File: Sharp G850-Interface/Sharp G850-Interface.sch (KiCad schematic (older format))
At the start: 26 parts

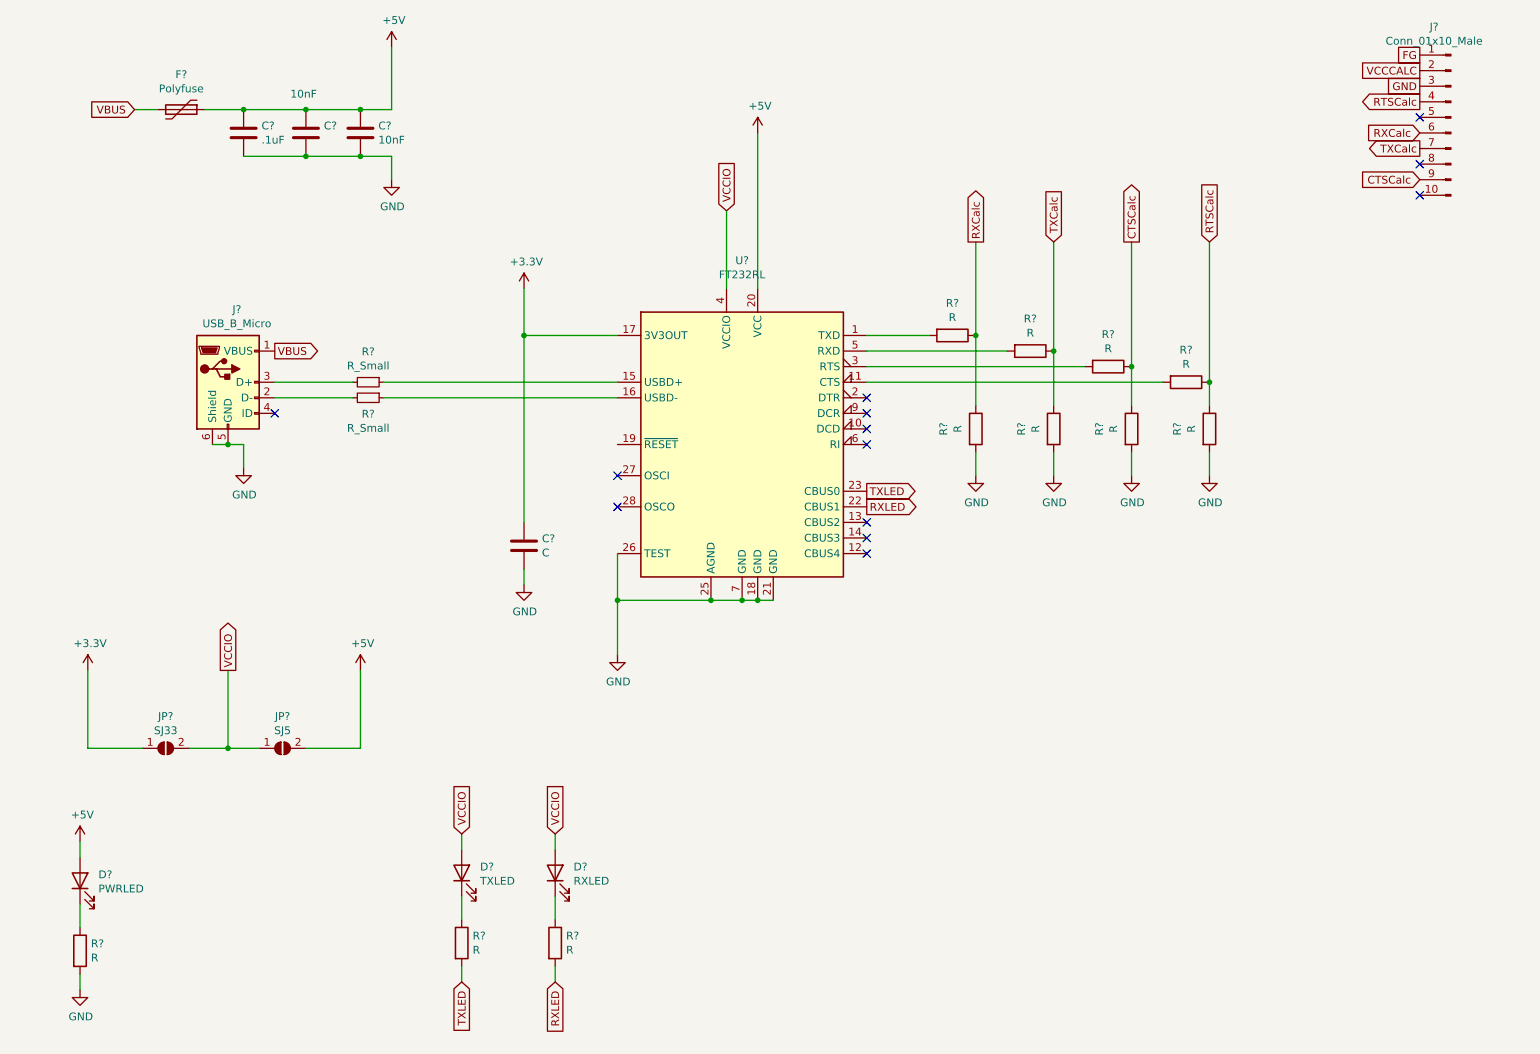
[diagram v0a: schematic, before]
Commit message: Finished G850 Schema
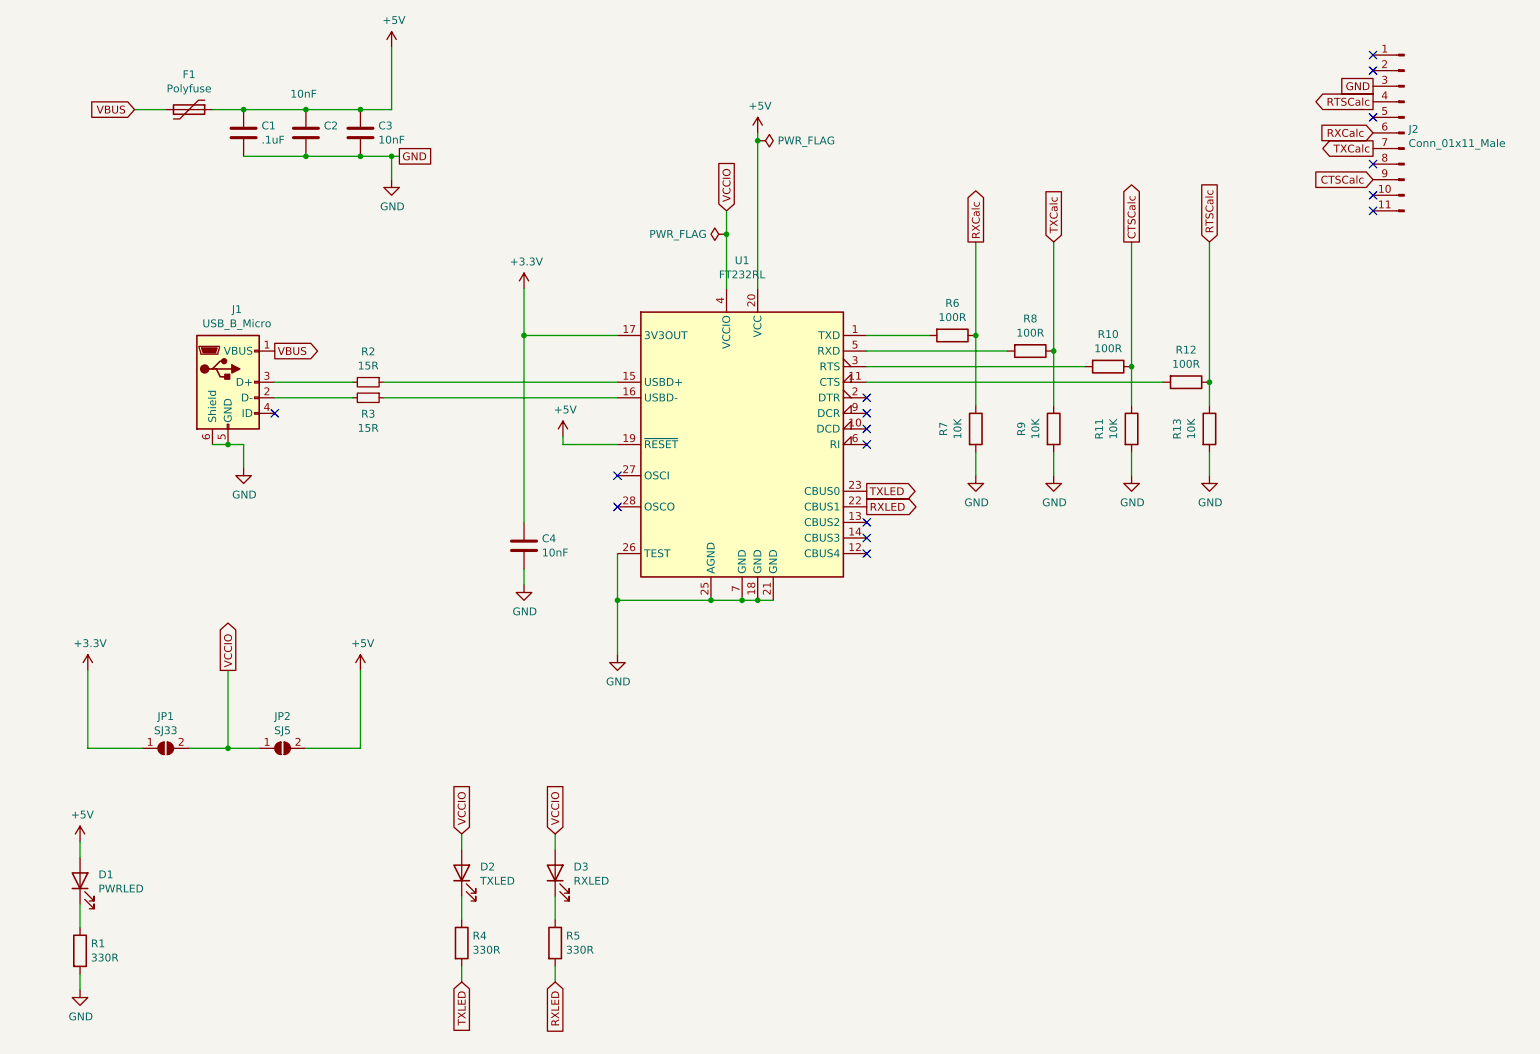
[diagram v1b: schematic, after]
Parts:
- removed J?: Conn_01x10_Male, symbol Connector:Conn_01x10_Male
- added J2: Conn_01x11_Male, symbol Connector:Conn_01x11_Male
- C4: renamed from C?; value C -> 10nF
- R1, R4, R5: renamed from R?; value R -> 330R
- R10, R12, R6, R8: renamed from R?; value R -> 100R
- R11, R13, R7, R9: renamed from R?; value R -> 10K
- R2, R3: renamed from R?; value R_Small -> 15R
- gave numbers to parts that had none: 11
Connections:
- net +5V: now also U1.19 (~RESET~)
- net CTSCalc: now also J2.9 (Pin_9)
- net GND: now also J2.3 (Pin_3)
- net RTSCalc: now also J2.4 (Pin_4)
- net RXCalc: now also J2.6 (Pin_6)
- net TXCalc: now also J2.7 (Pin_7)
- no-connect marks 13 -> 16
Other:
- moved on the sheet: F1

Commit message: Routage PCB Interface G850
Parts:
- added FB1: Ferrite_Bead_Small, Inductor_SMD:L_0805_2012Metric_Pad1.15x1.40mm_HandSolder, symbol Device:Ferrite_Bead_Small
- added J3: Conn_01x11_Male, Connector_PinHeader_2.54mm:PinHeader_1x11_P2.54mm_Vertical, symbol Connector:Conn_01x11_Male
- C1, C2, C3, C4: footprint (none) -> Capacitor_SMD:C_0805_2012Metric_Pad1.15x1.40mm_HandSolder
- D1, D2, D3: footprint (none) -> LED_SMD:LED_0805_2012Metric_Pad1.15x1.40mm_HandSolder
- F1: footprint (none) -> Resistor_SMD:R_1210_3225Metric_Pad1.42x2.65mm_HandSolder
- J1: footprint (none) -> Connector_USB:USB_Micro-B_Molex-105017-0001
- J2: footprint (none) -> Connector_PinHeader_2.54mm:PinHeader_1x11_P2.54mm_Horizontal
- JP1, JP2: footprint (none) -> Jumper:SolderJumper-2_P1.3mm_Open_RoundedPad1.0x1.5mm
- R1, R10, R11, R12, R13, R2, R3, R4, R5, R6, R7, R8, R9: footprint (none) -> Resistor_SMD:R_0805_2012Metric_Pad1.15x1.40mm_HandSolder
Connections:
- net +5V: now also FB1.1; no longer F1.1
- net CTSCalc: now also J3.9 (Pin_9)
- net GND: now also J3.3 (Pin_3)
- net RTSCalc: now also J3.4 (Pin_4)
- net RXCalc: now also J3.6 (Pin_6)
- net TXCalc: now also J3.7 (Pin_7)
- net USBD+: now reaches R2.1, U1.15 (USBD+)
- net USBD-: now reaches R3.1, U1.16 (USBD-)
- net D-: now reaches J1.2 (D-), R3.2
- net D+: now reaches J1.3 (D+), R2.2
- new net: F1.1, FB1.2
- no-connect marks 16 -> 22
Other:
- moved on the sheet: F1
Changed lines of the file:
@@
 F 0 "J1" H 2757 3567 50  0000 C CNN
 F 1 "USB_B_Micro" H 2757 3476 50  0000 C CNN
-F 2 "" H 2850 3050 50  0001 C CNN
+F 2 "Connector_USB:USB_Micro-B_Molex-105017-0001" H 2850 3050 50  0001 C CNN
 F 3 "~" H 2850 3050 50  0001 C CNN
 	1    2700 3100
@@
 L Device:Polyfuse F1
 U 1 1 5EB8FDB5
-P 2450 1350
-F 0 "F1" V 2225 1350 50  0000 C CNN
-F 1 "Polyfuse" V 2316 1350 50  0000 C CNN
-F 2 "" H 2500 1150 50  0001 L CNN
-F 3 "~" H 2450 1350 50  0001 C CNN
-	1    2450 1350
+P 2000 1350
+F 0 "F1" V 1775 1350 50  0000 C CNN
+F 1 "Polyfuse" V 1866 1350 50  0000 C CNN
+F 2 "Resistor_SMD:R_1210_3225Metric_Pad1.42x2.65mm_HandSolder" H 2050 1150 50  0001 L CNN
+F 3 "~" H 2000 1350 50  0001 C CNN
+	1    2000 1350
 	0    1    1    0
 $EndComp
@@
 F 0 "C1" H 2915 1546 50  0000 L CNN
 F 1 ".1uF" H 2915 1455 50  0000 L CNN
-F 2 "" H 2838 1350 50  0001 C CNN
+F 2 "Capacitor_SMD:C_0805_2012Metric_Pad1.15x1.40mm_HandSolder" H 2838 1350 50  0001 C CNN
 F 3 "~" H 2800 1500 50  0001 C CNN
 	1    2800 1500
@@
 F 0 "C2" H 3315 1546 50  0000 L CNN
 F 1 "10nF" H 3100 1750 50  0000 L CNN
-F 2 "" H 3238 1350 50  0001 C CNN
+F 2 "Capacitor_SMD:C_0805_2012Metric_Pad1.15x1.40mm_HandSolder" H 3238 1350 50  0001 C CNN
 F 3 "~" H 3200 1500 50  0001 C CNN
 	1    3200 1500
@@
 F 0 "C3" H 3665 1546 50  0000 L CNN
 F 1 "10nF" H 3665 1455 50  0000 L CNN
-F 2 "" H 3588 1350 50  0001 C CNN
+F 2 "Capacitor_SMD:C_0805_2012Metric_Pad1.15x1.40mm_HandSolder" H 3588 1350 50  0001 C CNN
 F 3 "~" H 3550 1500 50  0001 C CNN
 	1    3550 1500
@@
 Text GLabel 3000 2900 2    50   Output ~ 0
 VBUS
-Text GLabel 2100 1350 0    50   Input ~ 0
+Text GLabel 1650 1350 0    50   Input ~ 0
 VBUS
 Wire Wire Line
@@
 F 0 "JP2" H 3050 5655 50  0000 C CNN
 F 1 "SJ5" H 3050 5564 50  0000 C CNN
-F 2 "" H 3050 5450 50  0001 C CNN
+F 2 "Jumper:SolderJumper-2_P1.3mm_Open_RoundedPad1.0x1.5mm" H 3050 5450 50  0001 C CNN
 F 3 "~" H 3050 5450 50  0001 C CNN
 	1    3050 5450
@@
 F 0 "JP1" H 2300 5655 50  0000 C CNN
 F 1 "SJ33" H 2300 5564 50  0000 C CNN
-F 2 "" H 2300 5450 50  0001 C CNN
+F 2 "Jumper:SolderJumper-2_P1.3mm_Open_RoundedPad1.0x1.5mm" H 2300 5450 50  0001 C CNN
 F 3 "~" H 2300 5450 50  0001 C CNN
 	1    2300 5450
@@
 F 0 "R2" V 3404 3100 50  0000 C CNN
 F 1 "15R" V 3495 3100 50  0000 C CNN
-F 2 "" H 3600 3100 50  0001 C CNN
+F 2 "Resistor_SMD:R_0805_2012Metric_Pad1.15x1.40mm_HandSolder" H 3600 3100 50  0001 C CNN
 F 3 "~" H 3600 3100 50  0001 C CNN
 	1    3600 3100
@@
 F 0 "R3" V 3704 3200 50  0000 C CNN
 F 1 "15R" V 3795 3200 50  0000 C CNN
-F 2 "" H 3600 3200 50  0001 C CNN
+F 2 "Resistor_SMD:R_0805_2012Metric_Pad1.15x1.40mm_HandSolder" H 3600 3200 50  0001 C CNN
 F 3 "~" H 3600 3200 50  0001 C CNN
 	1    3600 3200
@@
 F 0 "D1" V 1789 6182 50  0000 R CNN
 F 1 "PWRLED" V 1698 6182 50  0000 R CNN
-F 2 "" H 1750 6300 50  0001 C CNN
+F 2 "LED_SMD:LED_0805_2012Metric_Pad1.15x1.40mm_HandSolder" H 1750 6300 50  0001 C CNN
 F 3 "~" H 1750 6300 50  0001 C CNN
 	1    1750 6300
@@
 F 0 "R1" H 1820 6796 50  0000 L CNN
 F 1 "330R" H 1820 6705 50  0000 L CNN
-F 2 "" V 1680 6750 50  0001 C CNN
+F 2 "Resistor_SMD:R_0805_2012Metric_Pad1.15x1.40mm_HandSolder" V 1680 6750 50  0001 C CNN
 F 3 "~" H 1750 6750 50  0001 C CNN
 	1    1750 6750
@@
 F 0 "D2" V 4239 6132 50  0000 R CNN
 F 1 "TXLED" V 4148 6132 50  0000 R CNN
-F 2 "" H 4200 6250 50  0001 C CNN
+F 2 "LED_SMD:LED_0805_2012Metric_Pad1.15x1.40mm_HandSolder" H 4200 6250 50  0001 C CNN
 F 3 "~" H 4200 6250 50  0001 C CNN
 	1    4200 6250
@@
 F 0 "R4" H 4270 6746 50  0000 L CNN
 F 1 "330R" H 4270 6655 50  0000 L CNN
-F 2 "" V 4130 6700 50  0001 C CNN
+F 2 "Resistor_SMD:R_0805_2012Metric_Pad1.15x1.40mm_HandSolder" V 4130 6700 50  0001 C CNN
 F 3 "~" H 4200 6700 50  0001 C CNN
 	1    4200 6700
@@
 F 0 "D3" V 4839 6132 50  0000 R CNN
 F 1 "RXLED" V 4748 6132 50  0000 R CNN
-F 2 "" H 4800 6250 50  0001 C CNN
+F 2 "LED_SMD:LED_0805_2012Metric_Pad1.15x1.40mm_HandSolder" H 4800 6250 50  0001 C CNN
 F 3 "~" H 4800 6250 50  0001 C CNN
 	1    4800 6250
@@
 F 0 "R5" H 4870 6746 50  0000 L CNN
 F 1 "330R" H 4870 6655 50  0000 L CNN
-F 2 "" V 4730 6700 50  0001 C CNN
+F 2 "Resistor_SMD:R_0805_2012Metric_Pad1.15x1.40mm_HandSolder" V 4730 6700 50  0001 C CNN
 F 3 "~" H 4800 6700 50  0001 C CNN
 	1    4800 6700
@@
 F 0 "R6" V 7143 2800 50  0000 C CNN
 F 1 "100R" V 7234 2800 50  0000 C CNN
-F 2 "" V 7280 2800 50  0001 C CNN
+F 2 "Resistor_SMD:R_0805_2012Metric_Pad1.15x1.40mm_HandSolder" V 7280 2800 50  0001 C CNN
 F 3 "~" H 7350 2800 50  0001 C CNN
 	1    7350 2800
@@
 F 0 "R8" V 7643 2900 50  0000 C CNN
 F 1 "100R" V 7734 2900 50  0000 C CNN
-F 2 "" V 7780 2900 50  0001 C CNN
+F 2 "Resistor_SMD:R_0805_2012Metric_Pad1.15x1.40mm_HandSolder" V 7780 2900 50  0001 C CNN
 F 3 "~" H 7850 2900 50  0001 C CNN
 	1    7850 2900
@@
 F 0 "R10" V 8143 3000 50  0000 C CNN
 F 1 "100R" V 8234 3000 50  0000 C CNN
-F 2 "" V 8280 3000 50  0001 C CNN
+F 2 "Resistor_SMD:R_0805_2012Metric_Pad1.15x1.40mm_HandSolder" V 8280 3000 50  0001 C CNN
 F 3 "~" H 8350 3000 50  0001 C CNN
 	1    8350 3000
@@
 F 0 "R12" V 8643 3100 50  0000 C CNN
 F 1 "100R" V 8734 3100 50  0000 C CNN
-F 2 "" V 8780 3100 50  0001 C CNN
+F 2 "Resistor_SMD:R_0805_2012Metric_Pad1.15x1.40mm_HandSolder" V 8780 3100 50  0001 C CNN
 F 3 "~" H 8850 3100 50  0001 C CNN
 	1    8850 3100
@@
 F 0 "R7" V 7293 3400 50  0000 C CNN
 F 1 "10K" V 7384 3400 50  0000 C CNN
-F 2 "" V 7430 3400 50  0001 C CNN
+F 2 "Resistor_SMD:R_0805_2012Metric_Pad1.15x1.40mm_HandSolder" V 7430 3400 50  0001 C CNN
 F 3 "~" H 7500 3400 50  0001 C CNN
 	1    7500 3400
@@
 F 0 "R9" V 7793 3400 50  0000 C CNN
 F 1 "10K" V 7884 3400 50  0000 C CNN
-F 2 "" V 7930 3400 50  0001 C CNN
+F 2 "Resistor_SMD:R_0805_2012Metric_Pad1.15x1.40mm_HandSolder" V 7930 3400 50  0001 C CNN
 F 3 "~" H 8000 3400 50  0001 C CNN
 	1    8000 3400
@@
 F 0 "R11" V 8293 3400 50  0000 C CNN
 F 1 "10K" V 8384 3400 50  0000 C CNN
-F 2 "" V 8430 3400 50  0001 C CNN
+F 2 "Resistor_SMD:R_0805_2012Metric_Pad1.15x1.40mm_HandSolder" V 8430 3400 50  0001 C CNN
 F 3 "~" H 8500 3400 50  0001 C CNN
 	1    8500 3400
@@
 F 0 "R13" V 8793 3400 50  0000 C CNN
 F 1 "10K" V 8884 3400 50  0000 C CNN
-F 2 "" V 8930 3400 50  0001 C CNN
+F 2 "Resistor_SMD:R_0805_2012Metric_Pad1.15x1.40mm_HandSolder" V 8930 3400 50  0001 C CNN
 F 3 "~" H 9000 3400 50  0001 C CNN
 	1    9000 3400
@@
 F 0 "C4" H 4715 4196 50  0000 L CNN
 F 1 "10nF" H 4715 4105 50  0000 L CNN
-F 2 "" H 4638 4000 50  0001 C CNN
+F 2 "Capacitor_SMD:C_0805_2012Metric_Pad1.15x1.40mm_HandSolder" H 4638 4000 50  0001 C CNN
 F 3 "~" H 4600 4150 50  0001 C CNN
 	1    4600 4150
@@
 F 0 "J2" H 10222 1524 50  0000 R CNN
 F 1 "Conn_01x11_Male" H 10222 1433 50  0000 R CNN
-F 2 "" H 10250 1500 50  0001 C CNN
+F 2 "Connector_PinHeader_2.54mm:PinHeader_1x11_P2.54mm_Horizontal" H 10250 1500 50  0001 C CNN
 F 3 "~" H 10250 1500 50  0001 C CNN
 	1    10250 1500
@@
 	2700 4950 2700 5450
 Wire Wire Line
-	2100 1350 2300 1350
-Wire Wire Line
-	2600 1350 2800 1350
-Connection ~ 2800 1350
+	1650 1350 1850 1350
 $Comp
 L power:PWR_FLAG #FLG0101
@@
 Wire Wire Line
 	5900 2150 5900 2000
+Text GLabel 10050 2450 0    50   UnSpc ~ 0
+GND
+Text GLabel 10050 2550 0    50   Output ~ 0
+RTSCalc
+Text GLabel 10050 2750 0    50   Input ~ 0
+RXCalc
+Text GLabel 10050 2850 0    50   Output ~ 0
+TXCalc
+Text GLabel 10050 3050 0    50   Input ~ 0
+CTSCalc
+NoConn ~ 10050 2650
+NoConn ~ 10050 2950
+NoConn ~ 10050 3150
+NoConn ~ 10050 2350
+NoConn ~ 10050 2250
+$Comp
+L Connector:Conn_01x11_Male J3
+U 1 1 5EC5BD70
+P 10250 2750
+F 0 "J3" H 10222 2774 50  0000 R CNN
+F 1 "Conn_01x11_Male" H 10222 2683 50  0000 R CNN
+F 2 "Connector_PinHeader_2.54mm:PinHeader_1x11_P2.54mm_Vertical" H 10250 2750 50  0001 C CNN
+F 3 "~" H 10250 2750 50  0001 C CNN
+	1    10250 2750
+	-1   0    0    -1
+$EndComp
+NoConn ~ 10050 3250
+$Comp
+L Device:Ferrite_Bead_Small FB1
+U 1 1 5EC5F7C4
+P 2550 1350
+F 0 "FB1" V 2313 1350 50  0000 C CNN
+F 1 "Ferrite_Bead_Small" V 2404 1350 50  0000 C CNN
+F 2 "Inductor_SMD:L_0805_2012Metric_Pad1.15x1.40mm_HandSolder" V 2480 1350 50  0001 C CNN
+F 3 "~" H 2550 1350 50  0001 C CNN
+	1    2550 1350
+	0    1    1    0
+$EndComp
+Wire Wire Line
+	2150 1350 2450 1350
+Wire Wire Line
+	2650 1350 2800 1350
+Connection ~ 2800 1350
+Text Label 3150 3100 0    50   ~ 0
+D+
+Text Label 3150 3200 0    50   ~ 0
+D-
+Text Label 4150 3100 0    50   ~ 0
+USBD+
+Text Label 4150 3200 0    50   ~ 0
+USBD-
 $EndSCHEMATC

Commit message: Finished PCB + Added gerber files
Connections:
- net FG: now reaches J2.1 (Pin_1)
- net FG: now also J3.1 (Pin_1)
- net DSRCalc: now reaches J2.10 (Pin_10)
- net DSRCalc: now also J3.10 (Pin_10)
- net CICalc: now reaches J2.11 (Pin_11)
- net CICalc: now also J3.11 (Pin_11)
- net VCCCalc: now reaches J2.2 (Pin_2)
- net VCCCalc: now also J3.2 (Pin_2)
- net DTRCalc: now reaches J2.5 (Pin_5)
- net DTRCalc: now also J3.5 (Pin_5)
- net CDCalc: now reaches J2.8 (Pin_8)
- net CDCalc: now also J3.8 (Pin_8)
- no-connect marks 22 -> 10
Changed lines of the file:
@@
 Text GLabel 10050 1800 0    50   Input ~ 0
 CTSCalc
-NoConn ~ 10050 1400
-NoConn ~ 10050 1700
-NoConn ~ 10050 1900
 $Comp
 L Device:R R6
@@
 	1    0    0    -1
 $EndComp
-NoConn ~ 10050 1100
 Wire Wire Line
 	5200 3500 4850 3500
@@
 	1    0    0    -1
 $EndComp
-NoConn ~ 10050 1000
 $Comp
 L Connector:Conn_01x11_Male J2
@@
 	-1   0    0    -1
 $EndComp
-NoConn ~ 10050 2000
 Wire Wire Line
 	3800 1650 3750 1650
@@
 Text GLabel 10050 3050 0    50   Input ~ 0
 CTSCalc
-NoConn ~ 10050 2650
-NoConn ~ 10050 2950
-NoConn ~ 10050 3150
-NoConn ~ 10050 2350
-NoConn ~ 10050 2250
-$Comp
-L Connector:Conn_01x11_Male J3
-U 1 1 5EC5BD70
-P 10250 2750
-F 0 "J3" H 10222 2774 50  0000 R CNN
-F 1 "Conn_01x11_Male" H 10222 2683 50  0000 R CNN
-F 2 "Connector_PinHeader_2.54mm:PinHeader_1x11_P2.54mm_Vertical" H 10250 2750 50  0001 C CNN
-F 3 "~" H 10250 2750 50  0001 C CNN
-	1    10250 2750
-	-1   0    0    -1
-$EndComp
-NoConn ~ 10050 3250
 $Comp
 L Device:Ferrite_Bead_Small FB1
@@
 Text Label 4150 3200 0    50   ~ 0
 USBD-
+$Comp
+L Connector:Conn_01x11_Male J3
+U 1 1 5EC5BD70
+P 10250 2750
+F 0 "J3" H 10222 2774 50  0000 R CNN
+F 1 "Conn_01x11_Male" H 10222 2683 50  0000 R CNN
+F 2 "Connector_PinHeader_2.54mm:PinHeader_1x11_P2.54mm_Vertical" H 10250 2750 50  0001 C CNN
+F 3 "~" H 10250 2750 50  0001 C CNN
+	1    10250 2750
+	-1   0    0    -1
+$EndComp
+Text GLabel 10050 1000 0    50   UnSpc ~ 0
+FG
+Text GLabel 10050 1100 0    50   UnSpc ~ 0
+VCCCalc
+Text GLabel 10050 1400 0    50   UnSpc ~ 0
+DTRCalc
+Text GLabel 10050 1700 0    50   UnSpc ~ 0
+CDCalc
+Text GLabel 10050 1900 0    50   UnSpc ~ 0
+DSRCalc
+Text GLabel 10050 2000 0    50   UnSpc ~ 0
+CICalc
+Text GLabel 10050 2250 0    50   UnSpc ~ 0
+FG
+Text GLabel 10050 2350 0    50   UnSpc ~ 0
+VCCCalc
+Text GLabel 10050 2650 0    50   UnSpc ~ 0
+DTRCalc
+Text GLabel 10050 2950 0    50   UnSpc ~ 0
+CDCalc
+Text GLabel 10050 3150 0    50   UnSpc ~ 0
+DSRCalc
+Text GLabel 10050 3250 0    50   UnSpc ~ 0
+CICalc
 $EndSCHEMATC
